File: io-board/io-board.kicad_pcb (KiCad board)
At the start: 4 copper layers, 75 x 54 mm, 81 parts, among them J1 BBPWR1, J10 BBPWR2, J2 BBPWR2, J3 Conn, J4 PWR, J5 In, J6 Out, J7 Headphone, J8 Conn, J9 BBPWR1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

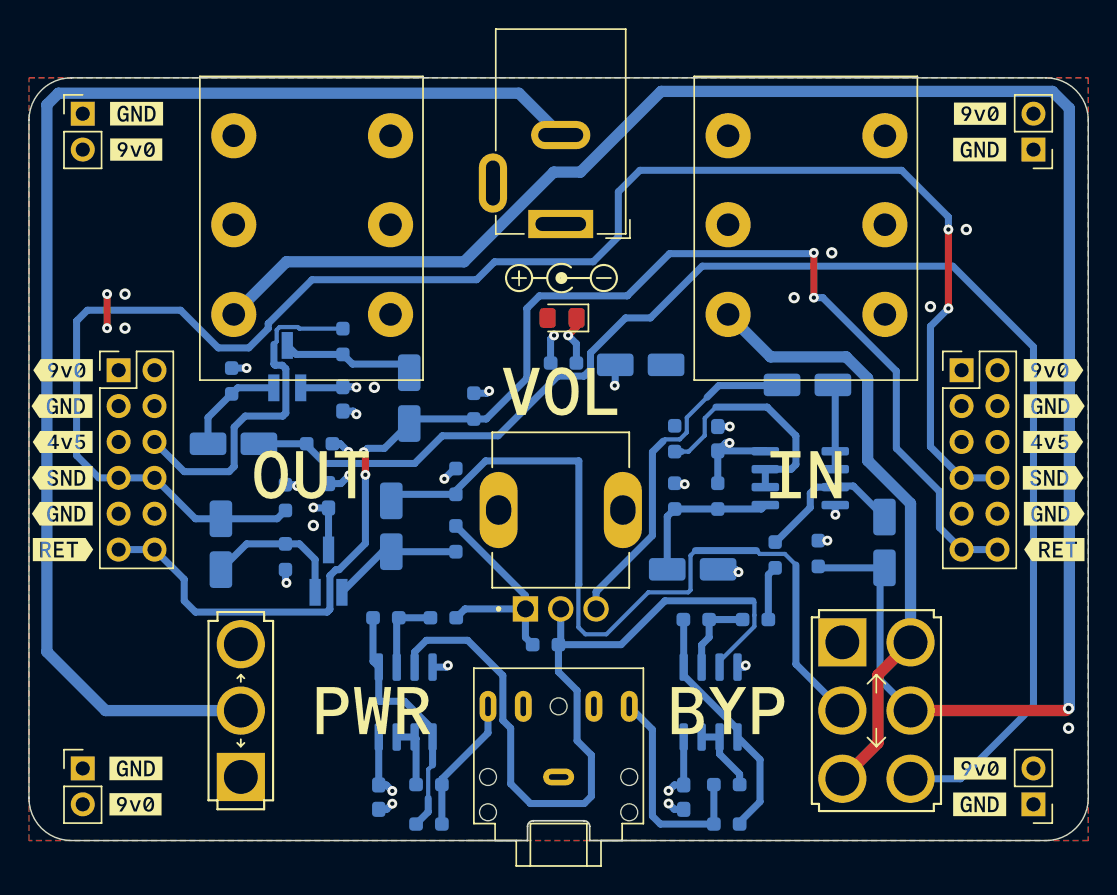
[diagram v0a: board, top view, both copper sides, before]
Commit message: Mounting holes
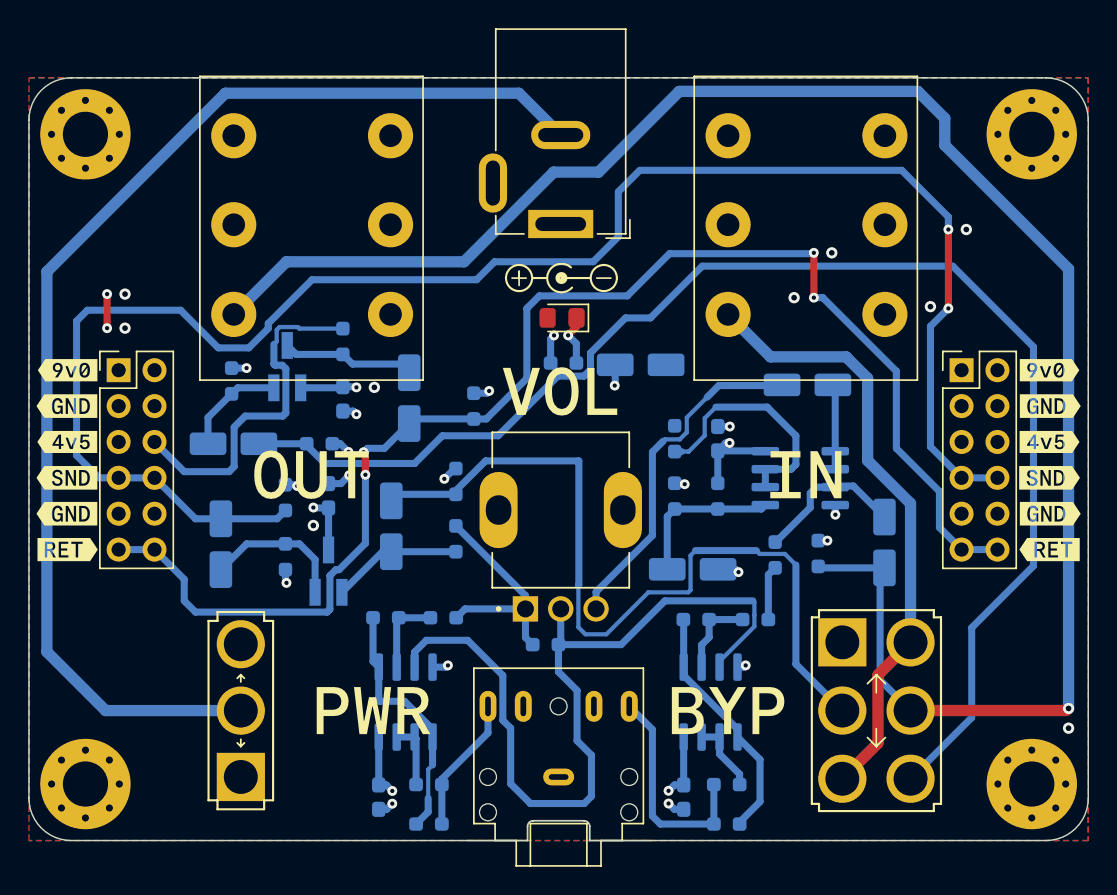
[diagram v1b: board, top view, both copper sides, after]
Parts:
- removed J1, J9: BBPWR1, Connector_PinHeader_2.54mm:PinHeader_1x02_P2.54mm_Vertical
- removed J10, J2: BBPWR2, Connector_PinHeader_2.54mm:PinHeader_1x02_P2.54mm_Vertical
- removed kibuzzard-65D620B4 (x2): G***, kibuzzard-65D620B4
- removed kibuzzard-65D620BA (x4): G***, kibuzzard-65D620BA
- removed kibuzzard-65D62103 (x2): G***, kibuzzard-65D62103
- added H1: TL, MountingHole:MountingHole_3.2mm_M3_Pad_Via, F.Cu at (64.0, 64.0)
- added H2: TR, MountingHole:MountingHole_3.2mm_M3_Pad_Via, F.Cu at (131.0, 64.0)
- added H3: BL, MountingHole:MountingHole_3.2mm_M3_Pad_Via, F.Cu at (64.0, 110.0)
- added H4: BR, MountingHole:MountingHole_3.2mm_M3_Pad_Via, F.Cu at (131.0, 110.0)
- moved kibuzzard-65D621F1 0.35 mm to (62.7, 83.2)
- moved kibuzzard-65D62054 0.34 mm to (132.3, 93.4)
- moved kibuzzard-65D621E9 0.33 mm to (62.7, 80.7)
- moved kibuzzard-65D621FF 0.33 mm to (62.7, 85.8)
- moved kibuzzard-65D6223E 0.33 mm to (62.7, 93.4)
- moved kibuzzard-65D6221F 0.32 mm to (62.7, 88.3)
- moved kibuzzard-65D6222D 0.32 mm to (62.7, 90.9)
- moved kibuzzard-65D61F98 0.28 mm to (132.3, 83.2)
- moved kibuzzard-65D61F98 0.28 mm to (132.3, 90.9)
- moved kibuzzard-65D62017 0.28 mm to (132.3, 80.7)
- moved kibuzzard-65D0BA3D 0.26 mm to (132.3, 88.3)
- moved kibuzzard-65D61F93 0.26 mm to (132.3, 85.8)
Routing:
- net +9V: track 92.1 -> 85.2 mm
- net /OutJack: track 135.8 -> 130.2 mm
- net /ReturnBuf: track 100.6 -> 98.5 mm

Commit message: Design
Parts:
- removed kibuzzard-65D622CD: G***, kibuzzard-65D622CD
- removed kibuzzard-65D62346: G***, kibuzzard-65D62346
- removed kibuzzard-65D625CE: G***, kibuzzard-65D625CE
- removed kibuzzard-65D62673: G***, kibuzzard-65D62673
- removed kibuzzard-65D62EE1: G***, kibuzzard-65D62EE1
- added G***: LOGO, LOGO, F.Cu at (65.5, 100.0)
- added G***: LOGO, LOGO, F.Cu at (129.5, 100.0)
- added kibuzzard-65D7710E: G***, kibuzzard-65D7710E, F.Cu at (115.0, 88.1)
- added kibuzzard-65D7712F: G***, kibuzzard-65D7712F, F.Cu at (80.0, 88.1)
- added kibuzzard-65D77151: G***, kibuzzard-65D77151, F.Cu at (97.6, 81.6)
- added kibuzzard-65D7717A: G***, kibuzzard-65D7717A, F.Cu at (84.4, 104.8)
- added kibuzzard-65D77183: G***, kibuzzard-65D77183, F.Cu at (109.5, 104.8)
- added kibuzzard-65D776CF: G***, kibuzzard-65D776CF, B.Cu at (97.5, 61.5)
- added kibuzzard-65D77819: G***, kibuzzard-65D77819, F.Cu at (66.2, 70.5)
- added kibuzzard-65D77824: G***, kibuzzard-65D77824, F.Cu at (128.8, 70.5)
- moved R21 7.41 mm to (112.9, 106.3), turned to -90 degrees
- moved R23 6.89 mm to (90.3, 106.2), turned to -90 degrees
- moved R20 1.85 mm to (111.3, 110.1), turned to 0 degrees
- moved U3 1.20 mm to (85.5, 104.1)
- moved C11 1.17 mm to (107.2, 110.1), turned to 0 degrees
- moved R17 1.01 mm to (89.8, 99.1)
- moved R19 1.00 mm to (84.8, 99.1)
- moved C12 0.93 mm to (84.5, 110.1), turned to 0 degrees
- moved R22 0.18 mm to (88.1, 110.1)
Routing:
- net /+4.5V: track 47.0 -> 244.8 mm
- net /HeadphoneL: track 15.8 -> 19.8 mm
- net Net-(R19-Pad2): track 17.9 -> 14.2 mm
- net Net-(R18-Pad2): track 17.3 -> 14.4 mm
- net /HeadphoneR: track 9.69 -> 6.98 mm

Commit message: graphics
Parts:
- removed the G*** at (65.5, 100.0)
- removed the G*** at (129.5, 100.0)
- added G***: LOGO, LOGO, F.Cu at (130.0, 102.0)
- added G***: LOGO, LOGO, F.Cu at (65.0, 102.0)
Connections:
- C1 pad 2: /Return -> /Send
- C2 pad 2: /Send -> /Return
- C5 pad 2: /SendBuf -> /ReturnBuf
- C6 pad 2: /ReturnBuf -> /SendBuf
- R2 pad 1: /Return -> /Send
- R3 pad 1: /Send -> /Return
- R8 pad 1: /SendBuf -> /ReturnBuf
- R9 pad 1: /ReturnBuf -> /SendBuf
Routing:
- net /ReturnBuf: track 98.5 -> 4.82 mm
- net /SendBuf: track 120.6 -> 202.3 mm
- net /Send: track 58.0 -> 4.83 mm, vias 0 -> 4
- net /Return: track 99.0 -> 58.4 mm, vias 4 -> 0

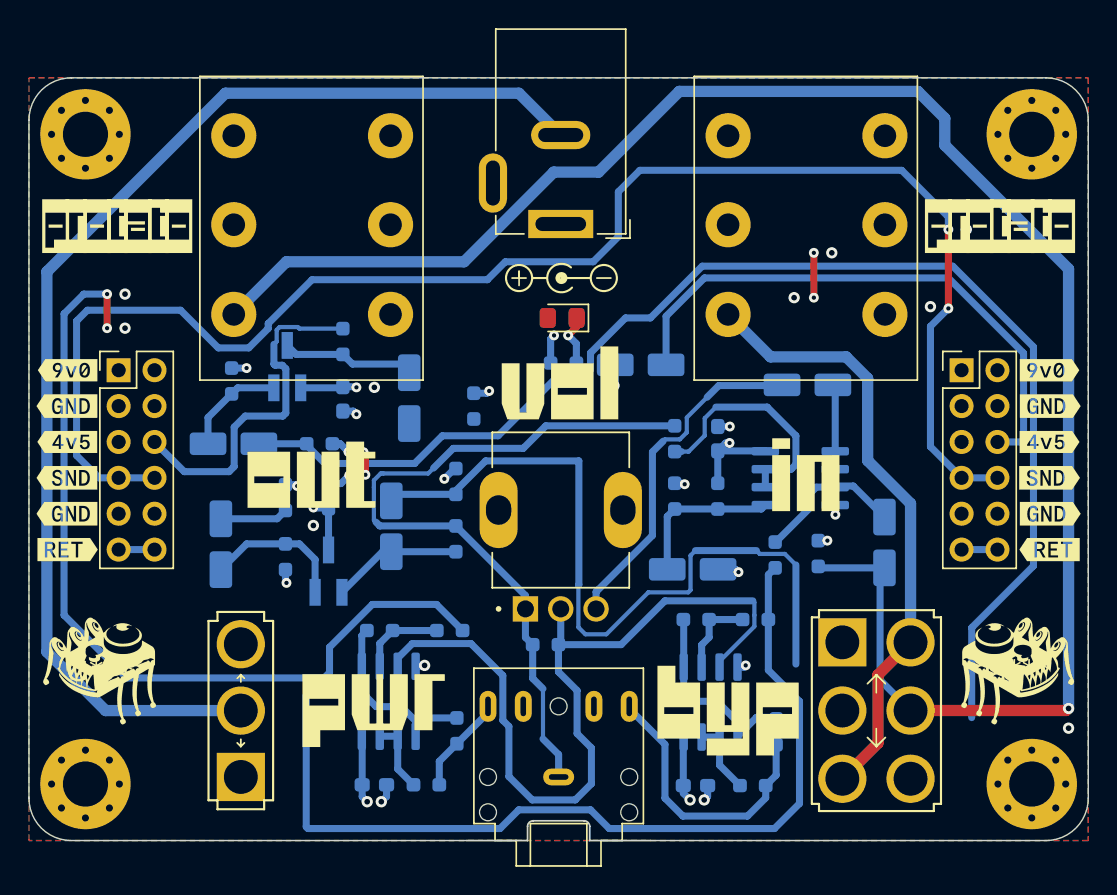
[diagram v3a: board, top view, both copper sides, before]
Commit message: Fixed buffers
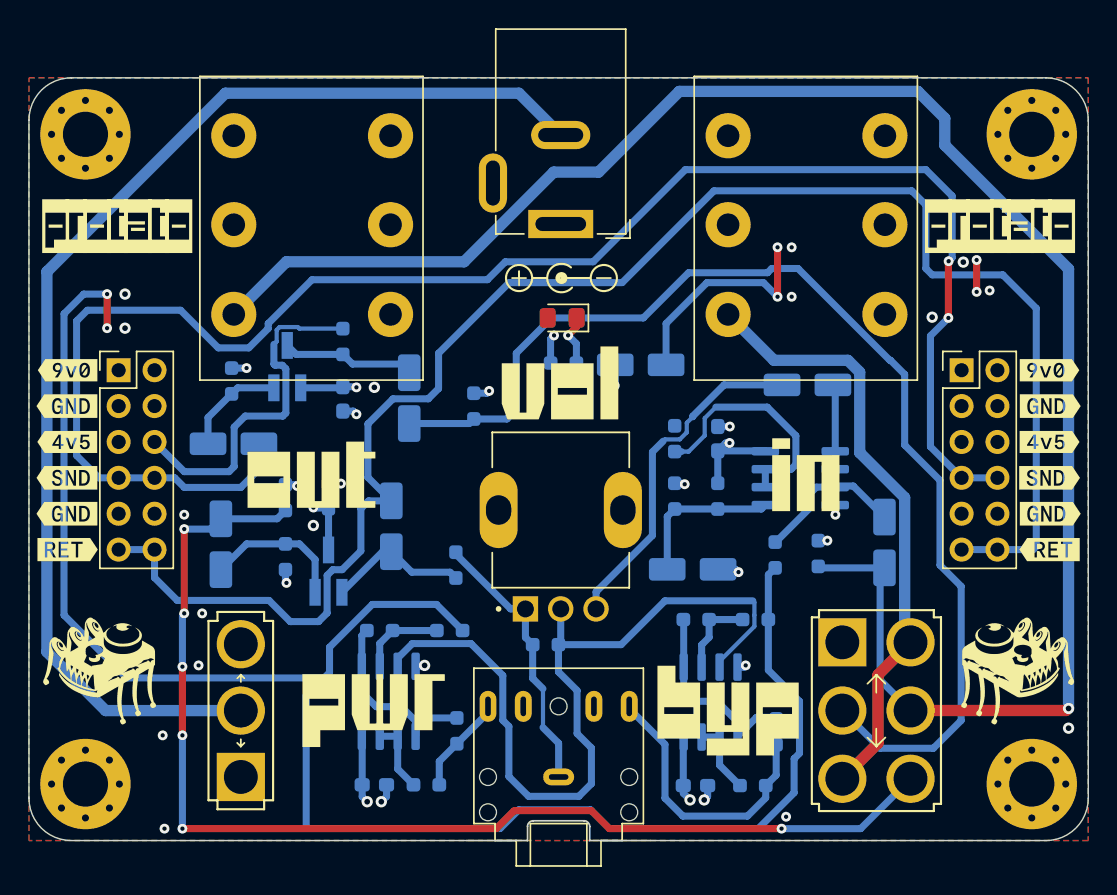
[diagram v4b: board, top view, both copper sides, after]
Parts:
- removed R3: 200K, Resistor_SMD:R_0603_1608Metric_Pad0.98x0.95mm_HandSolder
- removed R9: 10K, Resistor_SMD:R_0603_1608Metric_Pad0.98x0.95mm_HandSolder
- moved R5 1.86 mm to (90.2, 94.5)
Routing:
- net /SendBuf: track 202.3 -> 119.4 mm
- net /ReturnBuf: track 4.82 -> 83.0 mm, vias 0 -> 6
- net /Send: track 4.83 -> 81.6 mm, vias 4 -> 0
- net /Return: track 58.4 -> 119.5 mm
- net /+4.5V: track 244.8 -> 189.2 mm, vias 2 -> 6
- net GND: track 21.1 -> 17.7 mm, vias 28 -> 33
- net Net-(C2-Pad1): track 9.26 -> 10.0 mm

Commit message: Tag
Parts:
- removed kibuzzard-65D776CF: G***, kibuzzard-65D776CF
- added kibuzzard-65DA328B: G***, kibuzzard-65DA328B, B.Cu at (97.5, 61.8)
- added kibuzzard-65DA3308: G***, kibuzzard-65DA3308, B.Cu at (65.3, 101.2)
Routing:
- net GND: vias 33 -> 34

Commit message: wip
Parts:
- moved D1 0.25 mm to (97.5, 77.0)
- moved J4 0.15 mm to (97.5, 70.3)
- moved RV1 0.15 mm to (97.5, 90.6)
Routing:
- net /+4.5V: track 189.2 -> 190.0 mm
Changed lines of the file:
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@@
   )
   (footprint "LED_SMD:LED_0805_2012Metric_Pad1.15x1.40mm_HandSolder" (layer "F.Cu")
-    (at 97.75 77 180)
+    (at 97.5 77 180)
     (descr "LED SMD 0805 (2012 Metric), square (rectangular) end terminal, IPC_7351 nominal, (Body size source: https://docs.google.com/spreadsheets/d/1BsfQQcO9C6DZCsRaXUlFlo91Tg2WpOkGARC1WS5S8t0/edit?usp=sharing), generated with kicad-footprint-generator")
     (tags "LED handsolder")
@@
   )
   (footprint "Connector_BarrelJack:BarrelJack_GCT_DCJ200-10-A_Horizontal" locked (layer "F.Cu")
-    (at 97.65 70.35 180)
+    (at 97.5 70.35 180)
     (descr "Barrel jack connector (5.5 mm outer diameter, 2.05 inner diameter ), https://gct.co/files/drawings/dcj200-10.pdf")
     (tags "connector barrel jack")
@@
   )
   (footprint "R0904NB10KL-25KQ:V3_TRIM_R0904NB10KL-Keepout" locked (layer "F.Cu")
-    (at 97.65 90.6)
+    (at 97.5 90.6)
     (property "Sheetfile" "headphone.kicad_sch")
     (property "Sheetname" "Headphone Amp")
@@
       (polygon
         (pts
-          (xy 99.65 94.9)
-          (xy 95.65 94.9)
-          (xy 95.65 93.9)
-          (xy 99.65 93.9)
+          (xy 99.5 94.9)
+          (xy 95.5 94.9)
+          (xy 95.5 93.9)
+          (xy 99.5 93.9)
         )
       )
@@
       (polygon
         (pts
-          (xy 99.65 86.3)
-          (xy 95.65 86.3)
-          (xy 95.65 85.3)
-          (xy 99.65 85.3)
+          (xy 99.5 86.3)
+          (xy 95.5 86.3)
+          (xy 95.5 85.3)
+          (xy 99.5 85.3)
         )
       )
@@
     (attr board_only exclude_from_pos_files exclude_from_bom)
     (fp_text reference "kibuzzard-65DA328B" (at 0 4.059238) (layer "B.SilkS") hide
-      (effects (font (size 0 0)) (justify mirror))
+      (effects (font (size 0 0) (thickness 0.15)) (justify mirror))
     )
     (fp_text value "G***" (at 0 -4.059238) (layer "B.SilkS") hide
-      (effects (font (size 0 0)) (justify mirror))
+      (effects (font (size 0 0) (thickness 0.15)) (justify mirror))
     )
     (fp_poly (pts
@@
     (attr board_only exclude_from_pos_files exclude_from_bom)
     (fp_text reference "kibuzzard-65DA3308" (at 0 5.159211) (layer "B.SilkS") hide
-      (effects (font (size 0 0)) (justify mirror))
+      (effects (font (size 0 0) (thickness 0.15)) (justify mirror))
     )
     (fp_text value "G***" (at 0 -5.159211) (layer "B.SilkS") hide
-      (effects (font (size 0 0)) (justify mirror))
+      (effects (font (size 0 0) (thickness 0.15)) (justify mirror))
     )
     (fp_poly (pts
@@
   (segment (start 133.456 104.796) (end 133.604 104.648) (width 0.5) (layer "F.Cu") (net 12))
   (via (at 133.604 104.648) (size 0.8) (drill 0.4) (layers "F.Cu" "B.Cu") (net 12))
+  (segment (start 124.841 64.77) (end 133.604 73.533) (width 0.8) (layer "B.Cu") (net 12))
+  (segment (start 94.3 69.212742) (end 94.3 69.2) (width 0.8) (layer "B.Cu") (net 12))
+  (segment (start 94.3 69.2) (end 95.5 68) (width 0.8) (layer "B.Cu") (net 12))
   (segment (start 120.57 94.6945) (end 120.259 95.0055) (width 0.5) (layer "B.Cu") (net 12))
   (segment (start 120.259 102.638) (end 122.417 104.796) (width 0.5) (layer "B.Cu") (net 12))
-  (segment (start 106.045 60.96) (end 122.936 60.96) (width 0.8) (layer "B.Cu") (net 12))
+  (segment (start 90.487742 73.025) (end 94.3 69.212742) (width 0.8) (layer "B.Cu") (net 12))
   (segment (start 115.9835 94.6945) (end 115.88 94.591) (width 0.5) (layer "B.Cu") (net 12))
-  (segment (start 133.604 73.533) (end 133.604 104.648) (width 0.8) (layer "B.Cu") (net 12))
-  (segment (start 78.225 73.025) (end 90.805 73.025) (width 0.8) (layer "B.Cu") (net 12))
-  (segment (start 100.33 66.675) (end 106.045 60.96) (width 0.8) (layer "B.Cu") (net 12))
-  (segment (start 90.805 73.025) (end 97.155 66.675) (width 0.8) (layer "B.Cu") (net 12))
-  (segment (start 120.57 94.6945) (end 115.9835 94.6945) (width 0.5) (layer "B.Cu") (net 12))
-  (segment (start 120.259 95.0055) (end 120.259 102.638) (width 0.5) (layer "B.Cu") (net 12))
-  (segment (start 124.841 64.77) (end 133.604 73.533) (width 0.8) (layer "B.Cu") (net 12))
-  (segment (start 97.155 66.675) (end 100.33 66.675) (width 0.8) (layer "B.Cu") (net 12))
-  (segment (start 122.936 60.96) (end 124.841 62.865) (width 0.8) (layer "B.Cu") (net 12))
   (segment (start 124.841 62.865) (end 124.841 64.77) (width 0.8) (layer "B.Cu") (net 12))
+  (segment (start 100.5 68) (end 107.54 60.96) (width 0.8) (layer "B.Cu") (net 12))
   (segment (start 74.5 76.75) (end 78.225 73.025) (width 0.8) (layer "B.Cu") (net 12))
+  (segment (start 95.5 68) (end 100.5 68) (width 0.8) (layer "B.Cu") (net 12))
+  (segment (start 107.54 60.96) (end 122.936 60.96) (width 0.8) (layer "B.Cu") (net 12))
+  (segment (start 120.57 94.6945) (end 115.9835 94.6945) (width 0.5) (layer "B.Cu") (net 12))
+  (segment (start 122.936 60.96) (end 124.841 62.865) (width 0.8) (layer "B.Cu") (net 12))
+  (segment (start 120.259 95.0055) (end 120.259 102.638) (width 0.5) (layer "B.Cu") (net 12))
+  (segment (start 78.225 73.025) (end 90.487742 73.025) (width 0.8) (layer "B.Cu") (net 12))
+  (segment (start 133.604 73.533) (end 133.604 104.648) (width 0.8) (layer "B.Cu") (net 12))
   (segment (start 111.8575 90.527) (end 112.135 90.2495) (width 0.5) (layer "B.Cu") (net 13))
   (segment (start 108.768 90.527) (end 111.8575 90.527) (width 0.5) (layer "B.Cu") (net 13))
@@
   (segment (start 117.085 81.9075) (end 116.918 81.7405) (width 0.5) (layer "B.Cu") (net 14))
   (segment (start 117.085 87.7095) (end 117.085 86.4395) (width 0.5) (layer "B.Cu") (net 14))
-  (segment (start 100.15 96.395584) (end 104.14 92.405584) (width 0.5) (layer "B.Cu") (net 15))
-  (segment (start 104.14 92.405584) (end 104.14 86.487) (width 0.5) (layer "B.Cu") (net 15))
+  (segment (start 100 97.6) (end 100 96.5) (width 0.5) (layer "B.Cu") (net 15))
+  (segment (start 100 96.5) (end 104.14 92.36) (width 0.5) (layer "B.Cu") (net 15))
   (segment (start 106.07835 85.598) (end 105.029 85.598) (width 0.3) (layer "B.Cu") (net 15))
   (segment (start 104.14 86.487) (end 104.902 85.725) (width 0.5) (layer "B.Cu") (net 15))
@@
   (segment (start 106.573236 85.103114) (end 106.07835 85.598) (width 0.3) (layer "B.Cu") (net 15))
   (segment (start 107 84) (end 106.573236 84.426764) (width 0.3) (layer "B.Cu") (net 15))
-  (segment (start 100.15 97.6) (end 100.15 96.395584) (width 0.5) (layer "B.Cu") (net 15))
+  (segment (start 104.14 92.36) (end 104.14 86.487) (width 0.5) (layer "B.Cu") (net 15))
   (segment (start 113 75.5) (end 113 72) (width 0.5) (layer "F.Cu") (net 16))
-  (segment (start 127.095424 75.152424) (end 127.095424 72.898) (width 0.5) (layer "F.Cu") (net 16))
   (segment (start 65.532 77.724) (end 65.532 75.311) (width 0.5) (layer "F.Cu") (net 16))
+  (segment (start 127.095424 75.152424) (end 127.095424 72.136) (width 0.5) (layer "F.Cu") (net 16))
   (via (at 113 75.5) (size 0.7) (drill 0.3) (layers "F.Cu" "B.Cu") (net 16))
   (via (at 113 72) (size 0.7) (drill 0.3) (layers "F.Cu" "B.Cu") (net 16))
   (via (at 127.095424 75.152424) (size 0.7) (drill 0.3) (layers "F.Cu" "B.Cu") (free) (net 16))
-  (via (at 127.095424 72.898) (size 0.7) (drill 0.3) (layers "F.Cu" "B.Cu") (net 16))
+  (via (at 127.095424 72.136) (size 0.7) (drill 0.3) (layers "F.Cu" "B.Cu") (net 16))
   (via (at 65.532 75.311) (size 0.7) (drill 0.3) (layers "F.Cu" "B.Cu") (net 16))
   (via (at 65.532 77.724) (size 0.7) (drill 0.3) (layers "F.Cu" "B.Cu") (free) (net 16))
@@
   (segment (start 70.993 87.884) (end 68.89 85.781) (width 0.5) (layer "B.Cu") (net 16))
   (segment (start 79.1475 77.7565) (end 82.225 77.7565) (width 0.3) (layer "B.Cu") (net 16))
-  (segment (start 98.775 77.628) (end 98.775 77) (width 0.5) (layer "F.Cu") (net 17))
-  (segment (start 98.171 78.232) (end 98.775 77.628) (width 0.5) (layer "F.Cu") (net 17))
+  (segment (start 98.171 77.354) (end 98.525 77) (width 0.5) (layer "F.Cu") (net 17))
+  (segment (start 98.171 78.232) (end 98.171 77.354) (width 0.5) (layer "F.Cu") (net 17))
   (via (at 98.171 78.232) (size 0.7) (drill 0.3) (layers "F.Cu" "B.Cu") (net 17))
   (segment (start 98.7585 78.8195) (end 98.7585 80.193) (width 0.5) (layer "B.Cu") (net 17))
@@
   (segment (start 113.9665 87.7095) (end 112.135 87.7095) (width 0.5) (layer "B.Cu") (net 30))
   (segment (start 106.196 86.463) (end 106.704 86.463) (width 0.3) (layer "B.Cu") (net 30))
-  (segment (start 97.65 97.6) (end 97.65 99.9705) (width 0.5) (layer "B.Cu") (net 31))
+  (segment (start 97.5 100.1205) (end 97.4885 100.132) (width 0.5) (layer "B.Cu") (net 31))
   (segment (start 93.98 109.474) (end 93.98 105.918) (width 0.5) (layer "B.Cu") (net 31))
-  (segment (start 97.65 99.9705) (end 97.4885 100.132) (width 0.5) (layer "B.Cu") (net 31))
   (segment (start 111.36 98.843893) (end 111.36 98.044) (width 0.3) (layer "B.Cu") (net 31))
   (segment (start 101.925 100.132) (end 97.4885 100.132) (width 0.5) (layer "B.Cu") (net 31))
@@
   (segment (start 98.806 103.378) (end 98.806 106.426) (width 0.5) (layer "B.Cu") (net 31))
   (segment (start 108.895 101.308893) (end 111.36 98.843893) (width 0.3) (layer "B.Cu") (net 31))
+  (segment (start 97.5 97.75) (end 97.5 100.1205) (width 0.5) (layer "B.Cu") (net 31))
   (segment (start 87.142 100.056) (end 86.106 101.092) (width 0.5) (layer "B.Cu") (net 31))
   (segment (start 105.029 97.028) (end 101.925 100.132) (width 0.5) (layer "B.Cu") (net 31))
